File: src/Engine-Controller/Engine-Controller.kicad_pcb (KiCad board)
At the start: 4 copper layers, 101.6 x 50.8 mm, 60 parts, among them J1 Jumper_NO, P1 EJ508A, P2 USB, P3 SBH11-PBPC-D05-RA-BK, P4 0901471110, P5 66953-005LF, P6 Micro_SD_Card, P7 0901471110, U1 STM32H750VBTx, U2 LM22672MRE-5.0_NOPB, U3 LMS8117AMP-3.3_NOPB, U4 SN74LV07ADR, U5 SST25VF040B-50-4I-S2AE-T, U6 TPS2115APWR

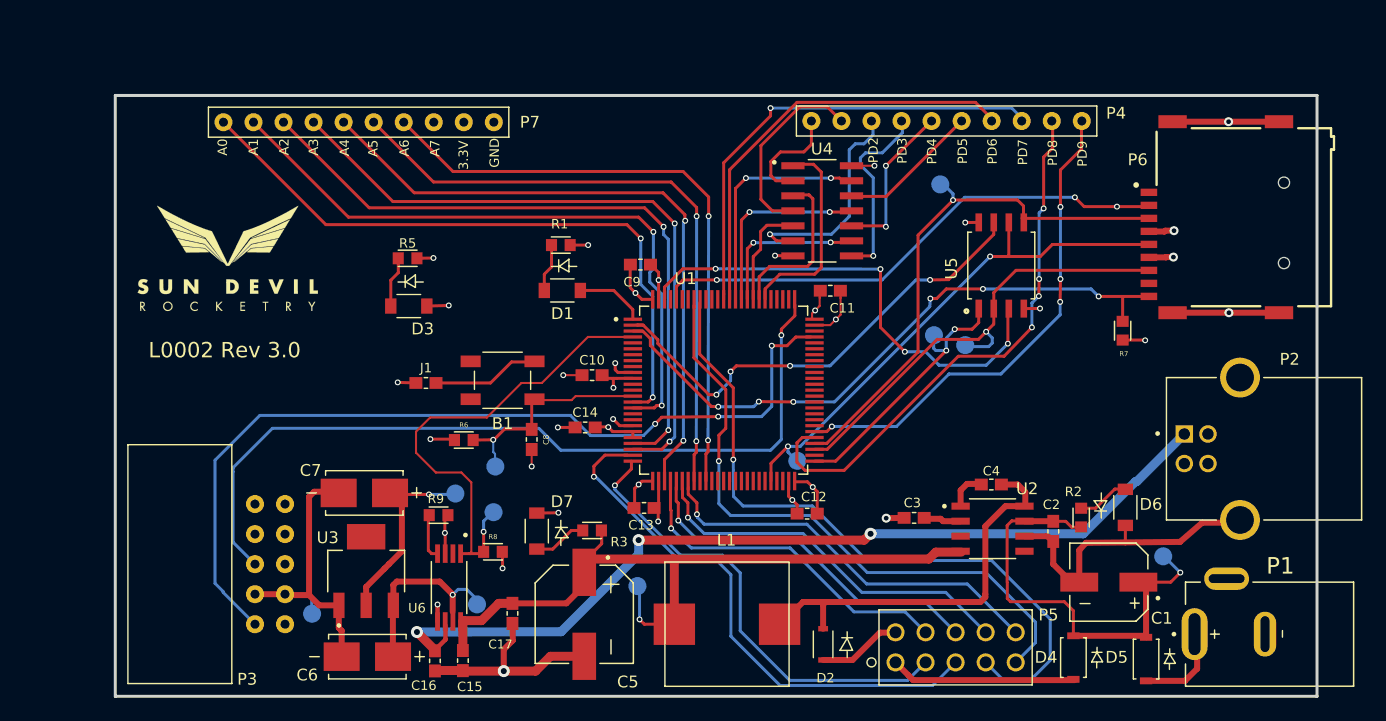
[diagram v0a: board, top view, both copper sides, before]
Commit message: finished routing rev3.0
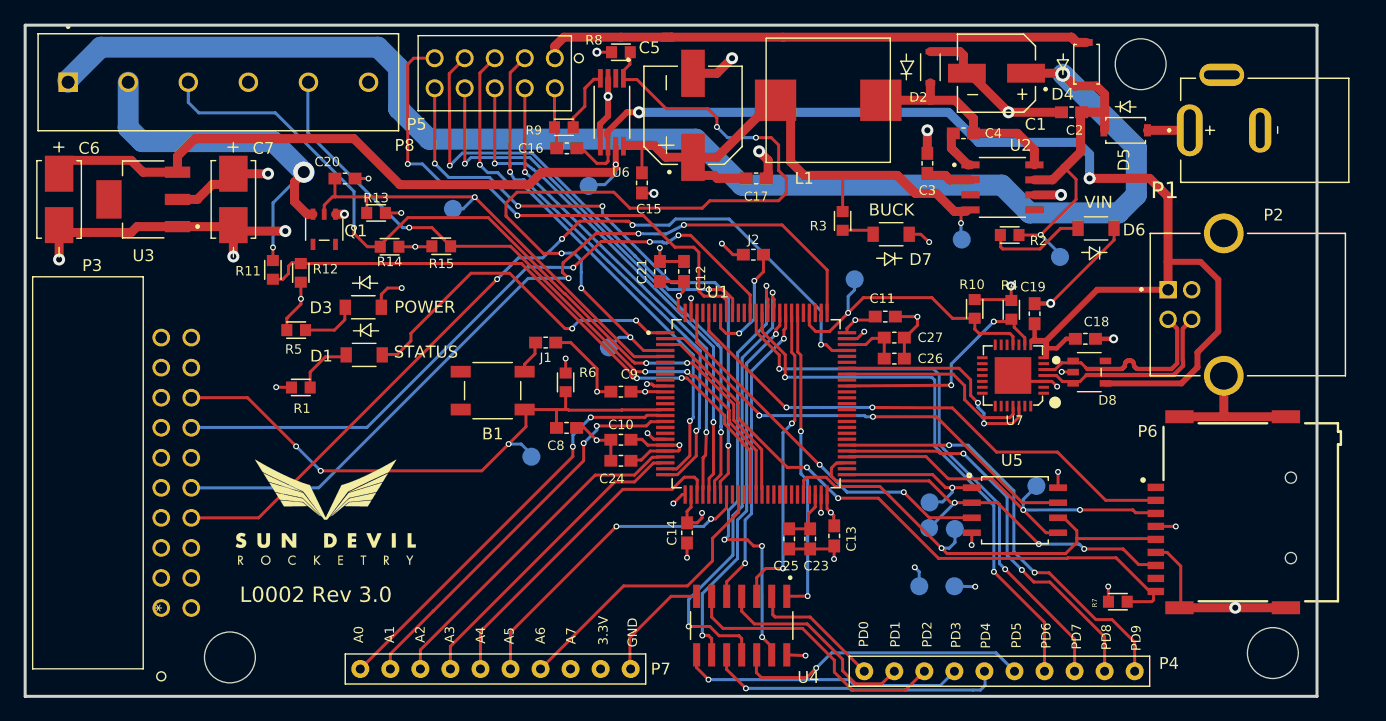
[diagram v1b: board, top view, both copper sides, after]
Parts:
- removed G***: LOGO, logo:Logo
- added C18: 1uF, Engine-Controller:CAP_0603, F.Cu at (183.6, 122.2)
- added C19: 0.1uF, Engine-Controller:CAP_0603, F.Cu at (179.3, 120.1)
- added C20: 1uF, Engine-Controller:CAP_0603, F.Cu at (121.0, 108.6)
- added C21: 4.7uF, Engine-Controller:CAP_0603, F.Cu at (147.7, 116.5)
- added C23: 2.2uF, Engine-Controller:CAP_0603, F.Cu at (160.4, 139.1)
- added C24: 1uF, Engine-Controller:CAP_0603, F.Cu at (144.3, 132.5)
- added C25: 2.2uF, Engine-Controller:CAP_0603, F.Cu at (158.6, 139.1)
- added C26: 2.2uF, Engine-Controller:CAP_0603, F.Cu at (167.5, 123.9)
- added C27: 2.2uF, Engine-Controller:CAP_0603, F.Cu at (167.5, 122.1)
- added D8: SP0504BAHTG_LTF, Engine-Controller:SP0504BAHTG, F.Cu at (183.9, 125.0)
- added H1: Mounting-Hole, Engine-Controller:MountingHole_4.3mm_M4_DIN965, F.Cu at (188.3, 99.0)
- added H2: Mounting-Hole, Engine-Controller:MountingHole_4.3mm_M4_DIN965, F.Cu at (111.3, 149.1)
- added H3: Mounting-Hole, Engine-Controller:MountingHole_4.3mm_M4_DIN965, F.Cu at (199.5, 148.7)
- added J2: Jumper_NO, Engine-Controller:Jumper-NO, F.Cu at (155.5, 115.1)
- added LOGO1: Logo, Engine-Controller:Logo, F.Cu at (119.4, 136.6)
- added P8: Solid Prop Cont, Engine-Controller:TE_282837-6, F.Cu at (110.3, 100.5)
- added Q1: TRANS_QS5K_ROM, Engine-Controller:QS5U17TR, F.Cu at (119.3, 112.9)
- added R10: 1k, Engine-Controller:RES_0603, F.Cu at (174.3, 119.6)
- added R11: 3k, Engine-Controller:RES_0603, F.Cu at (114.9, 116.3)
- added R12: 1k, Engine-Controller:RES_0603, F.Cu at (117.3, 116.6)
- added R13: 100k, Engine-Controller:RES_0603, F.Cu at (123.6, 111.5)
- added R14: 10k, Engine-Controller:RES_0603, F.Cu at (124.8, 114.4)
- added R15: 10k, Engine-Controller:RES_0603, F.Cu at (129.2, 114.4)
- added R4: 1k, Engine-Controller:RES_0603, F.Cu at (177.4, 119.7)
- added TP12: TP, Engine-Controller:TP, B.Cu at (164.1, 117.1)
- added TP13: TP, Engine-Controller:TP, B.Cu at (130.1, 111.2)
- added U7: CP2102-GMR(QFN28), Engine-Controller:CP2012-GMR, F.Cu at (177.5, 125.3)
- B1: value SW_PTS647SM38SMTR2LFS_CNK -> PTS647SM38SMTR2LFS
- P3: value SBH11-PBPC-D05-RA-BK -> SBH11-PBPC-D10-RA-BK; footprint Engine-Controller:SBH11-PBPC-D05-RA-BK -> Engine-Controller:SBH11-PBPC-D10-RA-BK
- moved P5 58.6 mm to (138.8, 98.5), turned to 180 degrees
- moved TP3 54.4 mm to (172.5, 143.1)
- moved D4 50.2 mm to (183.7, 99.0), turned to 90 degrees
- moved D2 49.6 mm to (170.5, 99.2), turned to 90 degrees
- moved P7 47.7 mm to (133.7, 150.1)
- moved P4 46.7 mm to (176.4, 150.3)
- moved C6 46.6 mm to (96.9, 110.4), turned to 270 degrees
- moved L1 45.1 mm to (161.9, 102.0)
- moved C16 44.7 mm to (139.8, 106.1), turned to 0 degrees
- moved D5 44.7 mm to (187.0, 104.5), turned to 0 degrees
- moved C1 44.1 mm to (176.1, 99.7)
- moved R8 43.6 mm to (144.3, 97.9), turned to 180 degrees
- moved C5 43.2 mm to (150.4, 103.3), turned to 90 degrees
- moved C15 43.1 mm to (146.1, 109.0)
- moved P1 42.6 mm to (195.1, 104.5)
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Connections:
- net /Connectors/PD0_BUF renamed PD0_BUF
- net /Connectors/PD1_BUF renamed PD1_BUF
- net /Connectors/PD2_BUF renamed PD2_BUF
- net /Connectors/PD3_BUF renamed PD3_BUF
- net /Connectors/PD4_BUF renamed PD4_BUF
- net /Connectors/PD5_BUF renamed PD5_BUF
- net /power/VIN renamed VIN
- B1 pad 1: /NRST -> NRST
- C8 pad 2: /NRST -> NRST
- P2 pad 2: Net-(P2-Pad2) -> /USB/D-
- P2 pad 3: Net-(P2-Pad3) -> /USB/D+
- R6 pad 2: /NRST -> NRST
- TP1 pad 1: /NRST -> NRST
- U1 pad 14: /NRST -> NRST
- U1 pad 37: Net-(U1-Pad37) -> E_CONT
- U1 pad 38: Net-(U1-Pad38) -> SP_CONT
- U1 pad 39: Net-(U1-Pad39) -> NOZ_CONT
- U1 pad 5: Net-(U1-Pad5) -> FIRE
- U1 pad 66: Net-(U1-Pad66) -> ~USB_RST
- U1 pad 68: Net-(U1-Pad68) -> RX_USB
- U1 pad 69: Net-(U1-Pad69) -> TX_USB
- U1 pad 79: Net-(U1-Pad79) -> ~USB_SUSPEND
- U1 pad 89: Net-(U1-Pad89) -> SWO
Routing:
- net VIN: track 38.2 -> 144.8 mm, vias 1 -> 2
- net NOZ_CONT: track 0.00 -> 70.8 mm, vias 0 -> 3
- net SWO: track 0.00 -> 57.7 mm, vias 0 -> 3
- net SP_CONT: track 0.00 -> 57.1 mm, vias 0 -> 3
- net E_CONT: track 0.00 -> 51.8 mm, vias 0 -> 2
- net NRST: track 0.00 -> 50.8 mm, vias 0 -> 3
- net /power/5V: track 16.3 -> 57.3 mm
- net FIRE: track 0.00 -> 40.2 mm, vias 0 -> 1
- net Net-(P8-Pad2): track 0.00 -> 33.7 mm, vias 0 -> 2
- net V_HEAD: track 15.8 -> 47.6 mm
- net A3: track 56.2 -> 26.1 mm, vias 2 -> 0
- net 5V_SRC: track 40.4 -> 70.2 mm, vias 1 -> 5
- net Earth: track 135.0 -> 164.3 mm, vias 22 -> 35
- net A6: track 52.5 -> 24.3 mm, vias 2 -> 0
- net A2: track 56.6 -> 28.4 mm, vias 2 -> 0
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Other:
- board size 101.6 x 50.8 mm -> 109.2 x 56.7 mm
- net class Power: clearance 0.254 -> 0.127
- net class USBData added: clearance 0.127, trace_width 0.254, via_dia 0.762, via_drill 0.4
- board text added: "BUCK"
- board text added: "E-match"
- board text added: "Nozzle"
- board text added: "POWER"
- board text added: "STATUS"
- board text added: "Solid Prop."

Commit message: fixed colors on connectors
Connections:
- net ~USB_RST renamed ~{USB_RST}
- net ~USB_SUSPEND renamed ~{USB_SUSPEND}
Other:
- net class Default removed
- net class Micro removed
- net class Power removed
- net class USBData removed

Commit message: Added minor changes
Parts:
- B1: value PTS647SM38SMTR2LFS -> SW_PTS647SM38SMTR2LFS_CNK
- D1: value 150120AS75000 -> LED_LTST-C150GKT_LTO
- D2: value RB160VAM-60TR -> DIO_RB160VAM_ROM
- D4, D5: value SM5819PL-TP -> SOD-123FL_MCC
- LOGO1: value Logo -> LOGO
- P3: value SBH11-PBPC-D10-RA-BK -> CONN20_D10-RA-BK_SUL
- P5: value 66953-005LF -> 66953-005LF_AMP
- U2: value LM22672MRE-5.0_NOPB -> VREG_LM5017MR/NOPB
- U4: value SN74LV07ADR -> SOIC127P600X175-14N
- U5: value SST25VF040B-50-4I-S2AE-T -> SOIC8_S2A_SST_MCH

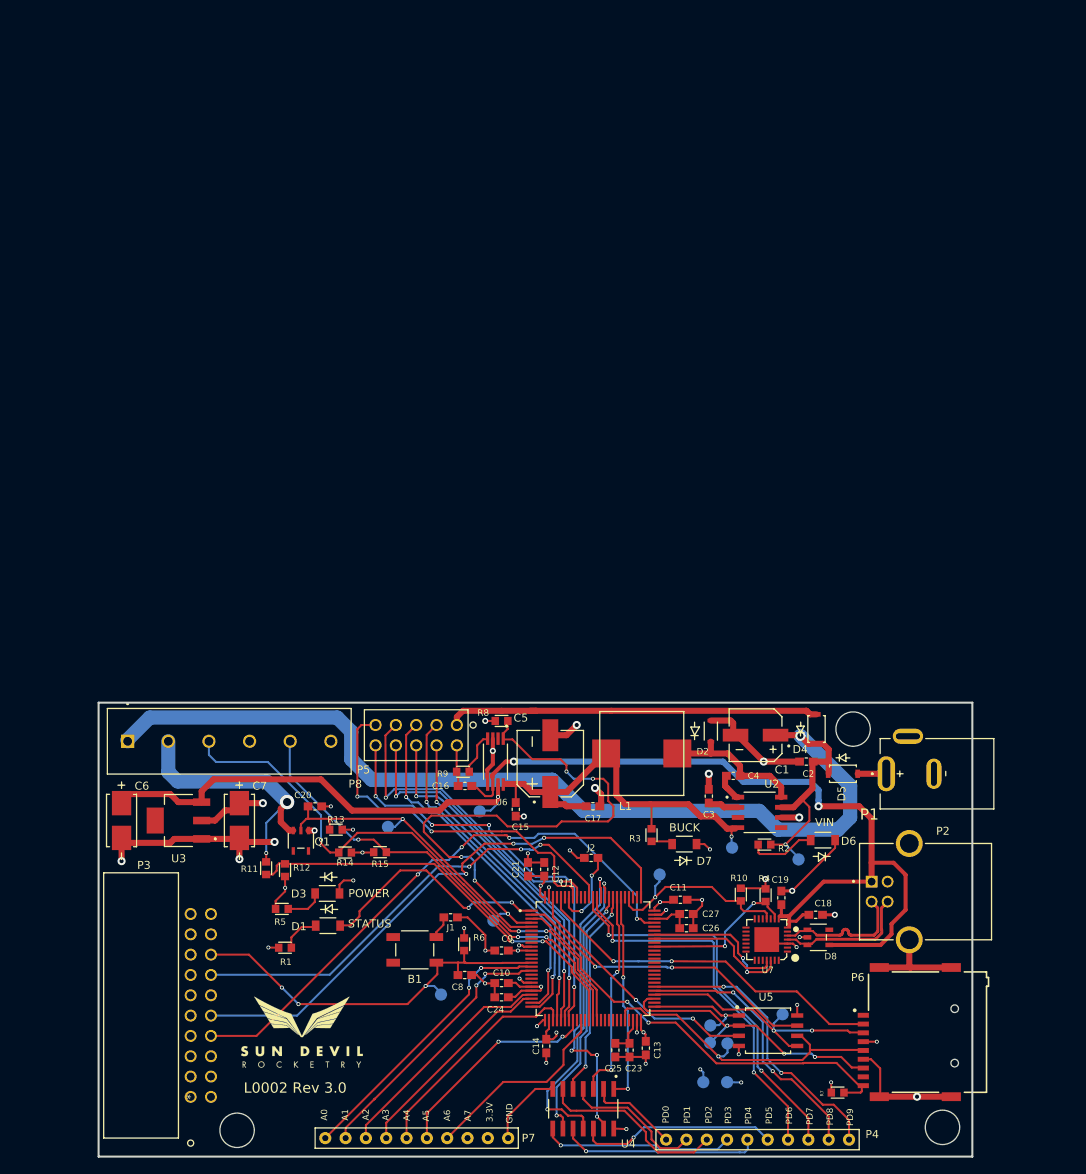
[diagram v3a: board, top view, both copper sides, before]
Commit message: removed unused traces in layout
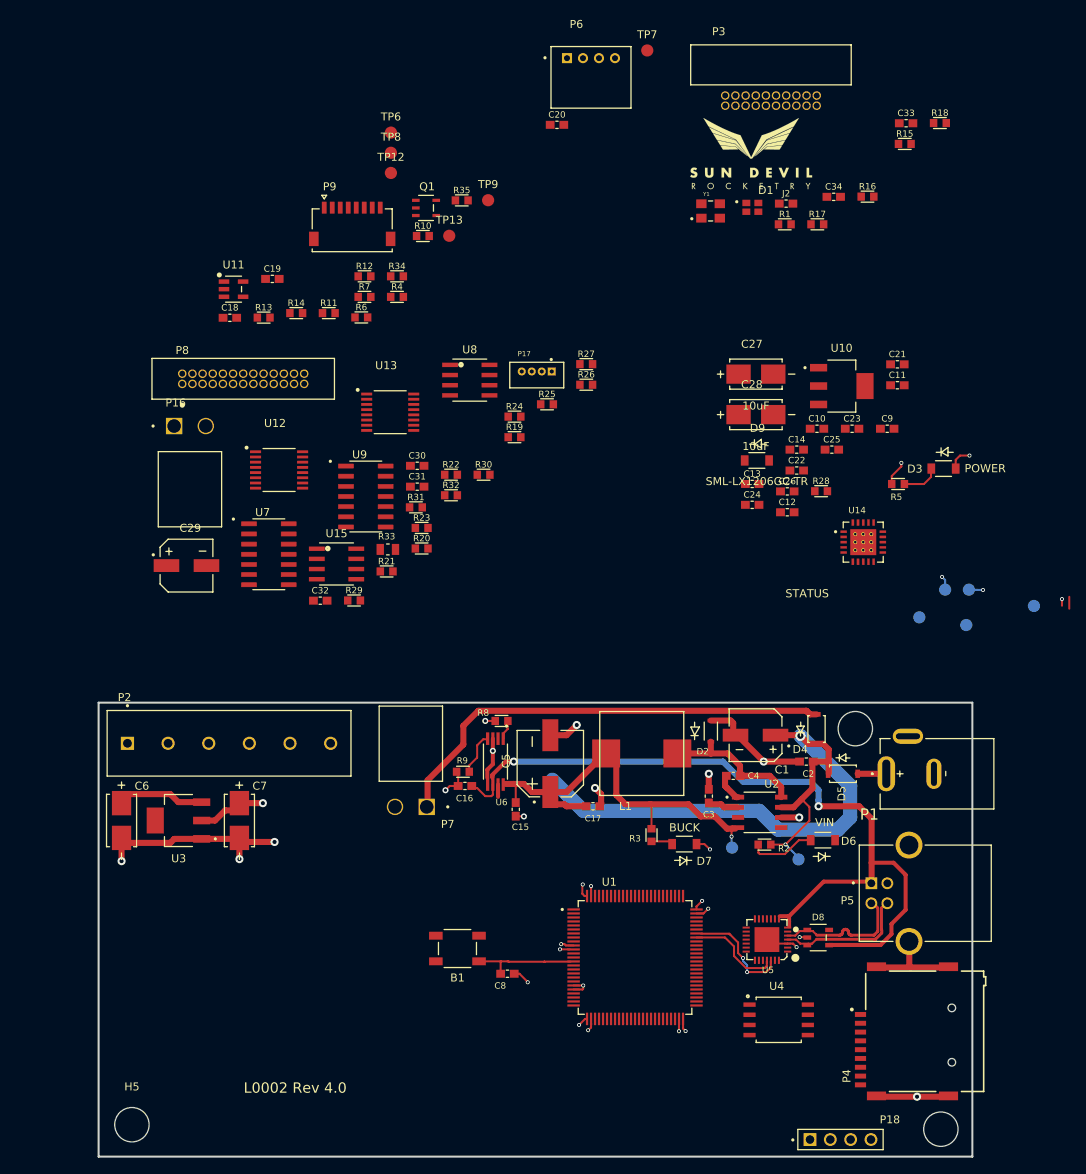
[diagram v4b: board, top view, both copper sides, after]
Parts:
- removed H1, H2, H3: Mounting-Hole, Engine-Controller:MountingHole_4.3mm_M4_DIN965
- removed J1: Jumper_NO, Engine-Controller:Jumper-NO
- removed LOGO1: LOGO, Engine-Controller:Logo
- added C22: 0.1u, Engine-Controller:CAP_0603, F.Cu at (181.2, 66.6)
- added C28: 10uF, Engine-Controller:CWR11HH106KB, F.Cu at (176.1, 59.7)
- added C29: 68uF, Engine-Controller:EEEFPV680XAP, F.Cu at (105.0, 78.5)
- added C30: 1uF, Engine-Controller:CAP_0603, F.Cu at (133.8, 66.0)
- added C31: 0.1uF, Engine-Controller:CAP_0603, F.Cu at (133.8, 68.7)
- added C32: 0.1uF, Engine-Controller:CAP_0603, F.Cu at (121.7, 82.9)
- added C33: 8pF, Engine-Controller:CAP_0603, F.Cu at (194.9, 23.2)
- added C34: 8pF, Engine-Controller:CAP_0603, F.Cu at (185.9, 32.4)
- added D9: SML-LX1206GC-TR, Engine-Controller:SML-LX1206GC-TR, F.Cu at (176.3, 65.4)
- added H4: Mounting-Hole, Engine-Controller:MountingHole_4.3mm_M4_DIN965, F.Cu at (188.6, 98.9)
- added H5: Mounting-Hole, Engine-Controller:MountingHole_4.3mm_M4_DIN965, F.Cu at (98.1, 148.4)
- added H6: Mounting-Hole, Engine-Controller:MountingHole_4.3mm_M4_DIN965, F.Cu at (199.3, 149.0)
- added LOGO2: Logo, Engine-Controller:Logo, F.Cu at (175.5, 26.8)
- added P16: 647676-2, Engine-Controller:647676-2, F.Cu at (103.4, 61.1)
- added P17: 0530470410, Engine-Controller:0530470410, F.Cu at (148.7, 54.3)
- added P18: PPTC041LFBN-RC, Engine-Controller:PPTC041LFBN-RC, F.Cu at (186.7, 150.3)
- added P9: 5015680807, Engine-Controller:5015680807, F.Cu at (125.7, 36.3)
- added R16: 82, Engine-Controller:RES_0603, F.Cu at (190.1, 32.4)
- added R17: 280, Engine-Controller:RES_0603, F.Cu at (183.8, 35.9)
- added R18: 100k, Engine-Controller:RES_0603, F.Cu at (199.1, 23.2)
- added R19: 1k, Engine-Controller:RES_0603, F.Cu at (146.0, 62.5)
- added R20: 1k, Engine-Controller:RES_0603, F.Cu at (134.4, 76.4)
- added R21: 1k, Engine-Controller:RES_0603, F.Cu at (130.0, 79.3)
- added R22: 1k, Engine-Controller:RES_0603, F.Cu at (138.0, 67.2)
- added R23: 1k, Engine-Controller:RES_0603, F.Cu at (134.4, 73.8)
- added R24: 1k, Engine-Controller:RES_0603, F.Cu at (146.0, 59.9)
- added R25: 1k, Engine-Controller:RES_0603, F.Cu at (150.0, 58.4)
- added R26: 1k, Engine-Controller:RES_0603, F.Cu at (154.9, 55.9)
- added R27: 1k, Engine-Controller:RES_0603, F.Cu at (154.9, 53.3)
- added R28: 240, Engine-Controller:RES_0603, F.Cu at (184.3, 69.2)
- added R29: 1M, Engine-Controller:RES_0603, F.Cu at (125.9, 82.9)
- added R30: 2M, Engine-Controller:RES_0603, F.Cu at (142.1, 67.2)
- added R31: 2k, Engine-Controller:RES_0603, F.Cu at (133.6, 71.2)
- added R32: 2k, Engine-Controller:RES_0603, F.Cu at (138.0, 69.7)
- added R33: 470, Engine-Controller:RES_0805, F.Cu at (130.1, 76.5)
- added R34: 10k, Engine-Controller:RES_0603, F.Cu at (131.3, 42.4)
- added R35: 10k, Engine-Controller:RES_0603, F.Cu at (139.4, 32.9)
- added U10: LMS8117AMP-3.3_NOPB, Engine-Controller:SOT-223, F.Cu at (186.9, 56.1)
- added U11: TS391IYLT, Engine-Controller:TS391IYLT, F.Cu at (110.8, 44.0)
- added U12: MAX4617EUE+T, Engine-Controller:max4617eue, F.Cu at (116.5, 66.6)
- added U13: MAX4617EUE+T, Engine-Controller:max4617eue, F.Cu at (130.4, 59.4)
- added U14: MCP96L01T-E_MX, Engine-Controller:MCP96L01T-E_MX, F.Cu at (189.6, 75.6)
- added U15: AD623ARZ-R7, Engine-Controller:AD623ARZ-R7, F.Cu at (123.7, 78.3)
- added U8: AD623ARZ-R7, Engine-Controller:AD623ARZ-R7, F.Cu at (140.4, 55.3)
- added U9: MC74HC4066ADG, Engine-Controller:MC74HC4066ADG, F.Cu at (127.4, 69.9)
- added Y1: ECS-240-18-33-JGN-TR, Engine-Controller:ECS-240-18-33-JGN-TR, F.Cu at (170.5, 34.2)
- B1: value SW_PTS647SM38SMTR2LFS_CNK -> PTS647SM38SMTR2LFS
- C10: value 0.1u -> 4.7uF
- C12: value 0.1u -> 1uF
- C17, C24: value 1uF -> 2.2uF
- C19: value 0.1uF -> 1uF
- C2: value 2.2uF -> 1uF
- C20: value 1uF -> 0.1uF
- C21: value 4.7uF -> 0.1u
- C27: value 2.2uF -> 10uF; footprint Engine-Controller:CAP_0603 -> Engine-Controller:CWR11HH106KB
- C3: value 1 uF -> 1uF
- C4: value 10 nF -> 10nF
- C5: footprint Engine-Controller:CAP_EEEFP1E151AL -> Engine-Controller:EEEFP1E151AL
- D1: value LED_LTST-C150GKT_LTO -> CLMVC-FKA-CL1D1L71BB7C3C3; footprint Engine-Controller:150120AS75000 -> Engine-Controller:CLMVC-FKA-CL1D1L71BB7C3C3
- D2: value DIO_RB160VAM_ROM -> RB160VAM-60TR
- D4, D5: value SOD-123FL_MCC -> SM5819PL-TP
- D8: value SP0504BAHTG_LTF -> SP0504BAHTG
- P2: value USB -> 282837-6; footprint Engine-Controller:USB-TypeB -> Engine-Controller:282837-6
- P3: value CONN20_D10-RA-BK_SUL -> 3220-20-0200-00; footprint Engine-Controller:SBH11-PBPC-D10-RA-BK -> Engine-Controller:3220-20-0200-00
- P4: value 0901471110 -> Micro_SD_Card; footprint Engine-Controller:0901471110 -> Engine-Controller:MEM2075-00-140-01-A
- P5: value 66953-005LF_AMP -> USB; footprint Engine-Controller:66953-005LF -> Engine-Controller:USB-TypeB
- P6: value Micro_SD_Card -> 140-504-415-000; footprint Engine-Controller:GCT_MEM2075-00-140-01-A -> Engine-Controller:140-504-415-000
- P7: value 0901471110 -> 647676-2; footprint Engine-Controller:0901471110 -> Engine-Controller:647676-2
- P8: value Solid Prop Cont -> 20021511-00026T4LF; footprint Engine-Controller:TE_282837-6 -> Engine-Controller:20021511-00026T4LF
- Q1: value TRANS_QS5K_ROM -> QS5U17TR
- R1: value 240 -> 68
- R10, R12: value 1k -> 10k
- R11: value 3k -> 10k
- R13: value 100k -> 4.7k
- R15, R7: value 10k -> 100k
- R4: value 1k -> 100k
- R6: value 10k -> 1k
- TP12, TP13, TP6, TP7, TP8, TP9: moved to F.Cu
- U2: value VREG_LM5017MR/NOPB -> LM22672MRE-5.0_NOPB
- U4: value SOIC127P600X175-14N -> SST25VF040B-50-4I-S2AE-T; footprint Engine-Controller:SN74LV07ADR -> Engine-Controller:SST25VF040B-50-4I-S2AE-T
- U5: value SOIC8_S2A_SST_MCH -> CP2102-GMR(QFN28); footprint Engine-Controller:SST25VF040B-50-4I-S2AE-T -> Engine-Controller:CP2012-GMR
- U7: value CP2102-GMR(QFN28) -> MC74HC4066ADG; footprint Engine-Controller:CP2012-GMR -> Engine-Controller:MC74HC4066ADG
- moved P3 144.7 mm to (178.0, 19.8), turned to 0 degrees
- moved P6 128.2 mm to (155.5, 17.5), turned to 0 degrees
- moved TP7 124.3 mm to (162.6, 14.1)
- moved TP8 119.0 mm to (130.5, 26.9)
- moved TP6 118.5 mm to (130.5, 24.4)
- moved R7 115.7 mm to (127.2, 44.9), turned to 0 degrees
- moved R15 110.2 mm to (194.8, 25.8)
- moved R1 109.9 mm to (179.8, 35.9), turned to 0 degrees
- moved TP9 108.2 mm to (142.7, 32.9)
- moved C18 104.6 mm to (110.4, 47.5), turned to 0 degrees
- moved D1 104.3 mm to (175.7, 33.7)
- moved C19 100.2 mm to (115.7, 42.7), turned to 0 degrees
- moved TP12 93.9 mm to (130.5, 29.4)
- moved R5 93.6 mm to (193.9, 68.3)
- moved D3 93.6 mm to (199.6, 66.4)
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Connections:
- net /power/V_JACK renamed Net-(D5-Pad2)
- net Net-(J2-Pad2) renamed BOOT
- B1 pad 2: Net-(B1-Pad2) -> unconnected-(B1-Pad2)
- B1 pad 3: Net-(B1-Pad3) -> Earth
- B1 pad 4: Net-(B1-Pad4) -> unconnected-(B1-Pad4)
- C18 pad 2: 5V_USB -> FIRE
- C20 pad 2: FIRE -> 5V_USB
- C23 pad 2: Net-(C23-Pad2) -> CAP1
- C24 pad 2: 3.3V -> CAP1
- C25 pad 2: Net-(C23-Pad2) -> CAP2
- C26 pad 2: Net-(C26-Pad2) -> CAP2
- C27 pad 1: Earth -> 5V
- C27 pad 2: Net-(C26-Pad2) -> Earth
- C6 pad 1: /power/5V -> 5V
- D1 pad 1: Net-(D1-Pad1) -> 3.3V
- D1 pad 2: /MCU_STATUS -> Net-(D1-Pad2)
- D8 pad 1: /USB/D- -> /Page2/D-
- D8 pad 3: /USB/D+ -> /Page2/D+
- D8 pad 5: Net-(D8-Pad5) -> unconnected-(D8-Pad5)
- P2 pad 1: 5V_USB -> VIN
- P2 pad 2: /USB/D- -> Net-(P2-Pad2)
- P2 pad 3: /USB/D+ -> SP_CONT
- P3 pad 1: Net-(P3-Pad1) -> 3.3V
- P3 pad 11: Net-(P3-Pad11) -> unconnected-(P3-Pad11)
- P3 pad 17: Net-(P3-Pad17) -> unconnected-(P3-Pad17)
- P3 pad 19: Net-(P3-Pad19) -> unconnected-(P3-Pad19)
- P3 pad 2: Net-(P3-Pad2) -> 3.3V
- P7 pad 1: A0 -> V_HEAD
- P7 pad 2: A1 -> Earth
- P8 pad 1: VIN -> 5V
- P8 pad 2: Net-(P8-Pad2) -> 5V
- P8 pad 3: NOZ_CONT -> 5V
- P8 pad 4: Earth -> 5V
- P8 pad 5: SP_CONT -> PT1+
- P8 pad 6: Earth -> PT1-
- Q1 pad 1: Earth -> FIRE
- Q1 pad 2: FIRE -> Earth
- Q1 pad 3: Net-(P8-Pad2) -> (no net)
- Q1 pad 5: (no net) -> Net-(P2-Pad2)
- R1 pad 1: Net-(D1-Pad1) -> STATUS_B
- R1 pad 2: Earth -> Net-(D1-Pad2)
- R10 pad 1: ~{USB_SUSPEND} -> 3.3V
- R10 pad 2: 3.3V -> SD_DETECT
- R11 pad 1: Net-(P8-Pad2) -> 3.3V
- R11 pad 2: E_CONT -> NOZ_CONT
- R12 pad 1: E_CONT -> 3.3V
- R12 pad 2: Earth -> SP_CONT
- R13 pad 1: FIRE -> ~{USB_RST}
- R13 pad 2: Earth -> 3.3V
- R14 pad 1: 3.3V -> ~{USB_SUSPEND}
- R14 pad 2: NOZ_CONT -> Earth
- R15 pad 1: 3.3V -> SWDIO
- R15 pad 2: SP_CONT -> 3.3V
- R4 pad 1: ~{USB_RST} -> Net-(P2-Pad2)
- R4 pad 2: 3.3V -> Earth
- R6 pad 2: NRST -> E_CONT
- R7 pad 1: SD_DETECT -> FIRE
- R7 pad 2: 3.3V -> Earth
- TP12 pad 1: ~{USB_SUSPEND} -> FLASH_MOSI
- TP13 pad 1: FIRE -> ~{USB_SUSPEND}
- TP4 pad 1: /power/5V -> 5V
- TP8 pad 1: FLASH_SCK -> FIRE
- TP9 pad 1: FLASH_MOSI -> FLASH_SCK
- U1 pad 1: /MCU_STATUS -> W_SCK
- U1 pad 12: Net-(U1-Pad12) -> OSC_IN
- U1 pad 13: Net-(U1-Pad13) -> OSC_OUT
- U1 pad 15: A0 -> PT
- U1 pad 16: A1 -> LC
- U1 pad 17: Net-(U1-Pad17) -> unconnected-(U1-Pad17)
- U1 pad 18: Net-(U1-Pad18) -> unconnected-(U1-Pad18)
- U1 pad 20: 3.3V -> A3.3V
- U1 pad 21: 3.3V -> A3.3V
- U1 pad 22: A2 -> W_TX
- U1 pad 23: A3 -> W_RX
- U1 pad 24: TX -> ValveCtrl_RX
- U1 pad 25: RX -> ValveCtrl_TX
- U1 pad 28: A4 -> unconnected-(U1-Pad28)
- U1 pad 29: SCK -> unconnected-(U1-Pad29)
- U1 pad 3: SD_DETECT -> W_MISO
- U1 pad 30: MISO -> unconnected-(U1-Pad30)
- U1 pad 31: MOSI -> unconnected-(U1-Pad31)
- U1 pad 32: SS -> unconnected-(U1-Pad32)
- U1 pad 33: A5 -> unconnected-(U1-Pad33)
- U1 pad 34: Net-(U1-Pad34) -> unconnected-(U1-Pad34)
- U1 pad 35: A6 -> W_SS
- U1 pad 36: Net-(U1-Pad36) -> unconnected-(U1-Pad36)
- U1 pad 4: 5V_SRC -> W_MOSI
- U1 pad 40: Net-(U1-Pad40) -> STATUS_R
- U1 pad 41: Net-(U1-Pad41) -> STATUS_G
- U1 pad 42: Net-(U1-Pad42) -> STATUS_B
- U1 pad 43: Net-(U1-Pad43) -> TC_ALERT
- U1 pad 44: Net-(U1-Pad44) -> TC_OC
- U1 pad 45: Net-(U1-Pad45) -> TC_SC
- U1 pad 47: Net-(U1-Pad47) -> unconnected-(U1-Pad47)
- U1 pad 48: Net-(C23-Pad2) -> CAP1
- U1 pad 52: Net-(U1-Pad52) -> SD_DETECT
- U1 pad 55: PD8 -> PT_GAIN7
- U1 pad 56: PD9 -> PT_MUX_A
- U1 pad 57: Net-(U1-Pad57) -> PT_MUX_B
- U1 pad 58: Net-(U1-Pad58) -> PT_MUX_C
- U1 pad 59: Net-(U1-Pad59) -> unconnected-(U1-Pad59)
- U1 pad 6: Net-(U1-Pad6) -> unconnected-(U1-Pad6)
- U1 pad 60: Net-(U1-Pad60) -> unconnected-(U1-Pad60)
- U1 pad 61: Net-(U1-Pad61) -> unconnected-(U1-Pad61)
- U1 pad 62: Net-(U1-Pad62) -> unconnected-(U1-Pad62)
- U1 pad 63: Net-(U1-Pad63) -> ~{USB_RST}
- U1 pad 64: Net-(U1-Pad64) -> ~{USB_SUSPEND}
- U1 pad 65: Net-(U1-Pad65) -> SD_DAT0
- U1 pad 66: ~{USB_RST} -> SD_DAT1
- U1 pad 67: Net-(U1-Pad67) -> unconnected-(U1-Pad67)
- U1 pad 7: Net-(U1-Pad7) -> unconnected-(U1-Pad7)
- U1 pad 70: Net-(U1-Pad70) -> unconnected-(U1-Pad70)
- U1 pad 71: Net-(U1-Pad71) -> unconnected-(U1-Pad71)
- U1 pad 73: Net-(C26-Pad2) -> CAP2
- U1 pad 77: Net-(U1-Pad77) -> unconnected-(U1-Pad77)
- U1 pad 78: Net-(U1-Pad78) -> SD_DAT2
- U1 pad 79: ~{USB_SUSPEND} -> SD_DAT3
- U1 pad 8: Net-(U1-Pad8) -> unconnected-(U1-Pad8)
- U1 pad 80: Net-(U1-Pad80) -> SD_CLK
- U1 pad 81: PD0 -> PT_GAIN0
- U1 pad 82: PD1 -> PT_GAIN1
- U1 pad 83: PD2 -> SD_CMD
- U1 pad 84: PD3 -> PT_GAIN2
- U1 pad 85: PD4 -> PT_GAIN3
- U1 pad 86: PD5 -> PT_GAIN4
- U1 pad 87: PD6 -> PT_GAIN5
- U1 pad 88: PD7 -> PT_GAIN6
- U1 pad 9: Net-(U1-Pad9) -> unconnected-(U1-Pad9)
- U1 pad 90: Net-(U1-Pad90) -> unconnected-(U1-Pad90)
- U1 pad 91: Net-(U1-Pad91) -> unconnected-(U1-Pad91)
- U1 pad 95: Net-(U1-Pad95) -> unconnected-(U1-Pad95)
- U1 pad 96: SD_SS -> unconnected-(U1-Pad96)
- U1 pad 97: Net-(U1-Pad97) -> 5V_SRC
- U2 pad 3: Net-(U2-Pad3) -> unconnected-(U2-Pad3)
- U2 pad 5: Net-(U2-Pad5) -> unconnected-(U2-Pad5)
- U3 pad 3: /power/5V -> 5V
- U4 pad 1: PD0 -> FLASH_SS
- U4 pad 2: PD0_BUF -> FLASH_MISO
- U4 pad 3: PD1 -> FLASH_WP
- U4 pad 4: PD1_BUF -> Earth
- U4 pad 5: PD2 -> FLASH_MOSI
- U4 pad 6: PD2_BUF -> FLASH_SCK
- U4 pad 7: Earth -> FLASH_HOLD
- U4 pad 8: PD3_BUF -> 3.3V
- U5 pad 1: FLASH_SS -> unconnected-(U5-Pad1)
- U5 pad 2: FLASH_MISO -> unconnected-(U5-Pad2)
- U5 pad 3: FLASH_WP -> Earth
- U5 pad 4: Earth -> /Page2/D+
- U5 pad 5: FLASH_MOSI -> /Page2/D-
- U5 pad 6: FLASH_SCK -> unconnected-(U5-Pad6)
- U5 pad 7: FLASH_HOLD -> 5V_USB
- U5 pad 8: 3.3V -> 5V_USB
- U6 pad 2: Net-(U6-Pad2) -> unconnected-(U6-Pad2)
- U6 pad 7: /power/5V -> 5V
- U7 pad 1: Net-(U7-Pad1) -> Net-(R27-Pad1)
- U7 pad 11: ~{USB_SUSPEND} -> Net-(R27-Pad1)
- U7 pad 12: Net-(U7-Pad12) -> PT_GAIN3
- U7 pad 13: Net-(U7-Pad13) -> PT_GAIN0
- U7 pad 14: Net-(U7-Pad14) -> 3.3V
- U7 pad 3: Earth -> Net-(R20-Pad1)
- U7 pad 4: /USB/D+ -> Net-(R27-Pad1)
- U7 pad 5: /USB/D- -> PT_GAIN1
- U7 pad 6: Net-(U7-Pad6) -> PT_GAIN2
- U7 pad 7: 5V_USB -> Earth
- U7 pad 8: 5V_USB -> Net-(R27-Pad1)
- U7 pad 9: ~{USB_RST} -> Net-(R21-Pad1)
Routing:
- net SWDIO: track 72.1 -> 0.00 mm, vias 4 -> 0
- net NOZ_CONT: track 70.8 -> 0.00 mm, vias 3 -> 0
- net SWCLK: track 69.1 -> 0.00 mm, vias 3 -> 0
- net 5V_SRC: track 70.2 -> 2.18 mm, vias 5 -> 0
- net Earth: track 164.3 -> 100.3 mm, vias 35 -> 23
- net VIN: track 144.8 -> 85.2 mm
- net SWO: track 57.7 -> 0.00 mm, vias 3 -> 0
- net /power/5V: track 57.3 -> 0.00 mm, vias 1 -> 0
- net SP_CONT: track 57.1 -> 0.00 mm, vias 3 -> 0
- net SD_DETECT: track 53.7 -> 0.00 mm, vias 2 -> 0
- net SS: track 52.8 -> 0.00 mm, vias 4 -> 0
- net E_CONT: track 51.8 -> 0.00 mm, vias 2 -> 0
- net PD7: track 48.5 -> 0.00 mm, vias 2 -> 0
- net PD6: track 47.6 -> 0.00 mm, vias 2 -> 0
- net MOSI: track 47.3 -> 0.00 mm, vias 2 -> 0
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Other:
- board text added: "L0002 Rev 4.0"
- board text removed: "3.3V"
- board text removed: "A0"
- board text removed: "A1"
- board text removed: "A2"
- board text removed: "A3"
- board text removed: "A4"
- board text removed: "A5"
- board text removed: "A6"
- board text removed: "A7"
- board text removed: "GND"
- board text removed: "L0002 Rev 3.0"
- board text removed: "MISO"
- board text removed: "MOSI"
- board text removed: "PD0"
- board text removed: "PD1"
- board text removed: "PD2"
- board text removed: "PD3"
- board text removed: "PD4"
- board text removed: "PD5"
- board text removed: "PD6"
- board text removed: "PD7"
- board text removed: "PD8"
- board text removed: "PD9"
- board text removed: "RX"
- board text removed: "SCK"
- board text removed: "SCL"
- board text removed: "SDA"
- board text removed: "SS"
- board text removed: "TX"
